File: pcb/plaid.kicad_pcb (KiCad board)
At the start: 2 copper layers, 228 x 98 mm, 139 parts, among them J1 USB_OTG, J2 AVR_ISP_6, J3 Conn_01x04, J4 GS2, J5 GS2, SW1 SW_Push, SW10 SW_Push, SW11 SW_Push, SW12 SW_Push, SW13 SW_Push, SW14 SW_Push, SW15 SW_Push, SW16 SW_Push, SW17 SW_Push, SW18 SW_Push, SW19 SW_Push, SW2 SW_Push, SW20 SW_Push, SW21 SW_Push, SW22 SW_Push, SW23 SW_Push, SW24 SW_Push, SW25 SW_Push, SW26 SW_Push, SW27 SW_Push, SW28 SW_Push, SW29 SW_Push, SW3 SW_Push, SW30 SW_Push, SW31 SW_Push, SW32 SW_Push, SW33 SW_Push, SW34 SW_Push, SW35 SW_Push, SW36 SW_Push, SW37 SW_Push, SW38 SW_Push, SW39 SW_Push, SW4 SW_Push, SW40 SW_Push, SW41 SW_Push, SW42 SW_Push, SW43 SW_Push, SW44 SW_Push, SW45 SW_Push, SW46 SW_Push, SW47 SW_Push, SW48 SW_Push, SW49 SW_Push, SW5 SW_Push, SW50 RESET, SW51 BOOT, SW6 SW_Push, SW7 SW_Push, SW8 SW_Push, SW9 SW_Push, U1 ATMEGA328-PU, Y1 16MHz

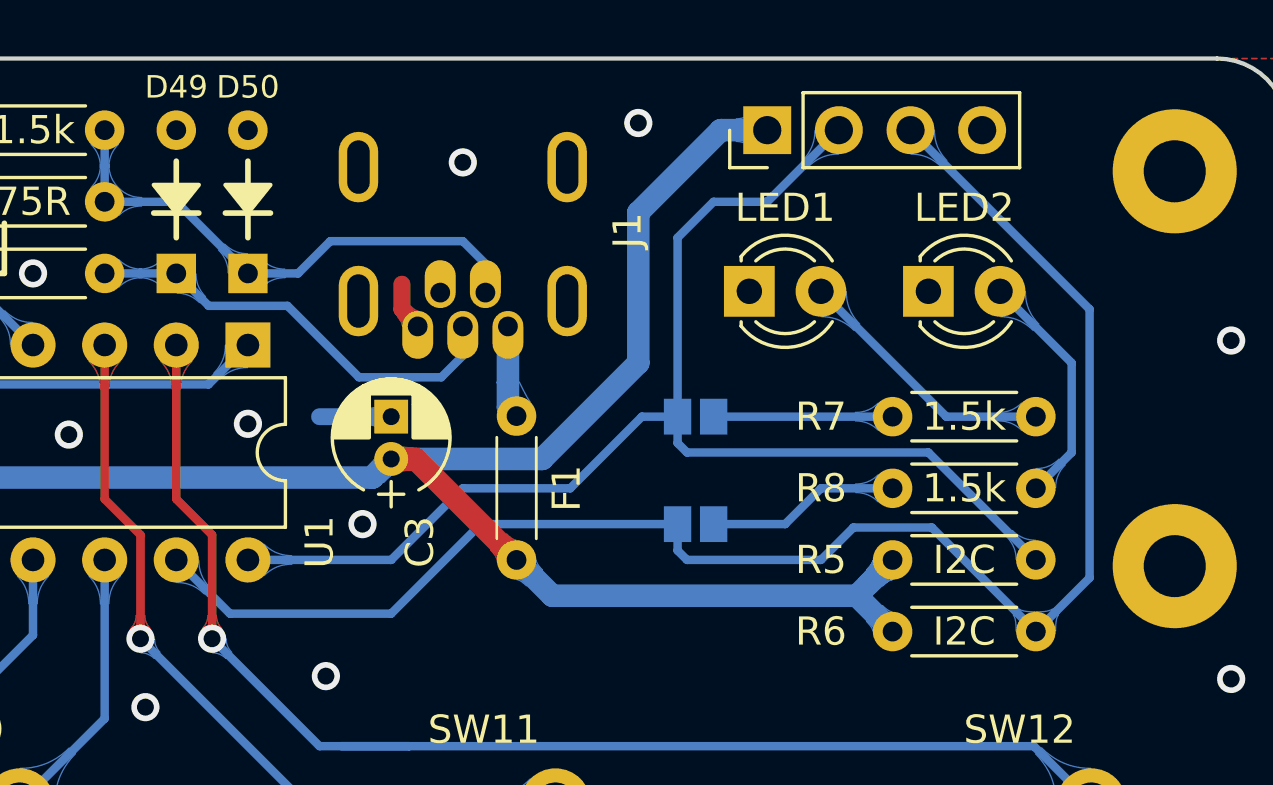
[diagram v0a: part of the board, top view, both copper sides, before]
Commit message: Replace Mini USB connector with USB-C
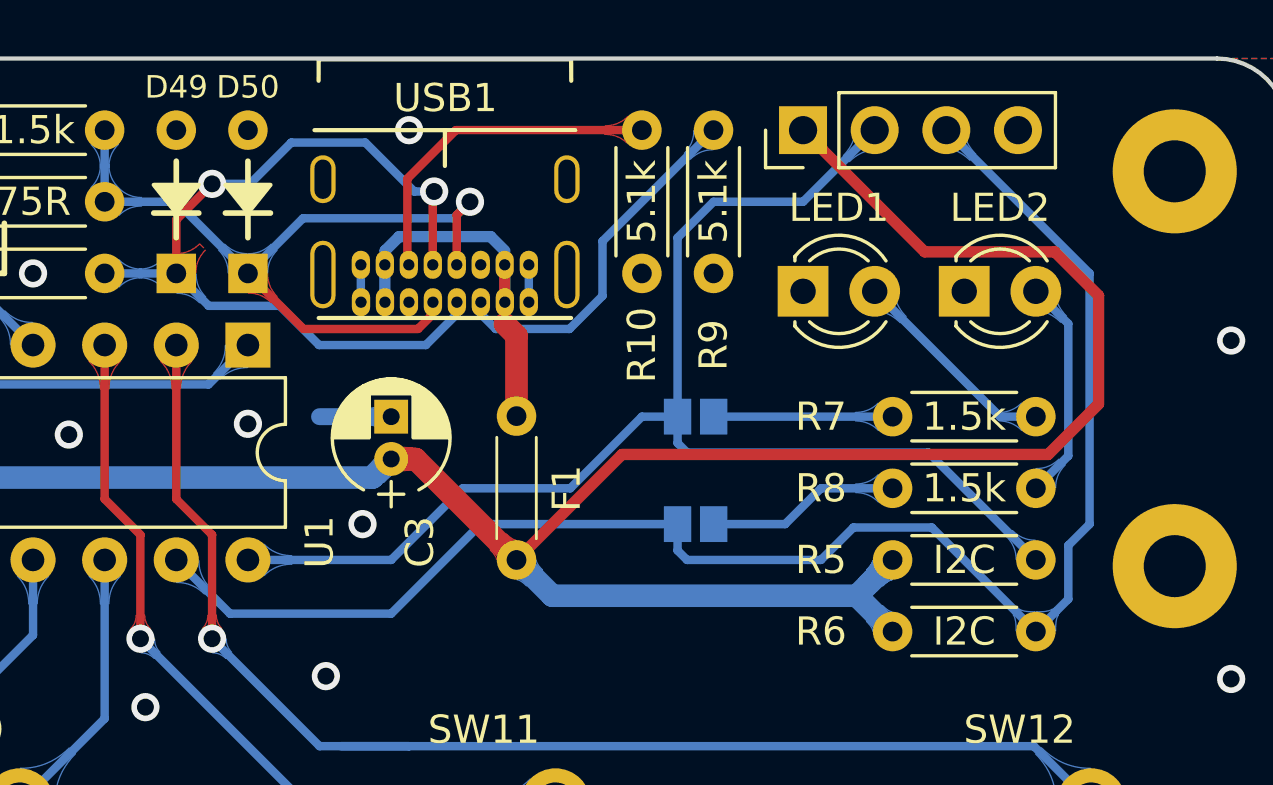
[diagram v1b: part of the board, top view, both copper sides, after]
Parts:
- removed J1: USB_OTG, dm9_conn:USB_MINIB_Akizuki_MUSB-5BF01AS
- added R10: 5.1k, Resistor_THT:R_Axial_DIN0204_L3.6mm_D1.6mm_P5.08mm_Horizontal, F.Cu at (255.1, 57.6)
- added R9: 5.1k, Resistor_THT:R_Axial_DIN0204_L3.6mm_D1.6mm_P5.08mm_Horizontal, F.Cu at (257.6, 57.6)
- added USB1: USB_C_GCT_USB4085-Type-C, plaid_silk:USB_C_GCT_USB4085, F.Cu at (248.1, 52.5)
- C3: value 10u -> 4.7u
- moved LED1 1.90 mm to (260.8, 58.3)
- moved LED2 1.27 mm to (266.5, 58.3)
- moved J3 1.27 mm to (260.8, 52.5)
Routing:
- net +5V: track 127.6 -> 146.0 mm
- net Net-(D49-Pad1): track 15.6 -> 29.9 mm, vias 0 -> 2
- net Net-(R9-Pad2): track 0.00 -> 12.9 mm
- net Net-(R10-Pad2): track 0.00 -> 12.1 mm
- net Net-(F1-Pad1): track 3.31 -> 12.9 mm
- net Net-(D50-Pad1): track 18.9 -> 28.0 mm, vias 0 -> 1
- net Net-(LED1-Pad2): track 9.46 -> 7.56 mm
- net /i2c_SCL: track 46.3 -> 47.6 mm
- net GND: track 8.83 -> 9.76 mm, vias 79 -> 78
- net Net-(LED2-Pad2): track 8.56 -> 7.94 mm
- net /i2c_SDA: track 56.9 -> 56.3 mm
- added copper zone on B.Cu, net /i2c_SCL
- added copper zone on B.Cu, net Net-(D49-Pad1)
- added copper zone on B.Cu, net Net-(D50-Pad1)
- added copper zone on B.Cu, net Net-(LED1-Pad2)
- added copper zone on B.Cu, net Net-(LED2-Pad2)
- added copper zone on F.Cu, net Net-(R10-Pad2)
- added copper zone on B.Cu, net Net-(R9-Pad2)
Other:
- net class Power: trace_width 0.8 -> 0.4
